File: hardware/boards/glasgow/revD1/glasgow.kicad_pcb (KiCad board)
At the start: 6 copper layers, 95 x 55 mm, 775 parts, among them J1 USB-C, J10 P1, J11 CLK_EXT, J12 FPGA_TP, J2 SWD, J3 COM, J4 SYNC, J5 JTAG, J6 LVDS, J7 P1, J8 P1, J9 P1, Q1 AO3401, Q2 AO3400, SW1 RST, U1 BL24C256A-SFRC, U10 74AXP1T45, U11 XccelaOPI, U12 XccelaOPI, U13 TLV62569PDRL, U14 TLV62569PDRL, U15 TLV61070ADBV, U16 APX811-40UG-7, U17 TLV77525DRL, U18 TLV62569PDRL, U19 TPS7A2033, U2 CY7C68013A-56LTX, U20 TPS22917DBV, U21 DAC43204, U22 LMR54406, U23 SY7208CABC, U24 TCA6416APW, U25 TCA6416APW, U26 74AXP1T45, U27 74AXP1T45, U28 TPS629203, U29 74AXP1T45, U3 TMP112xxDRL, U30 74AXP1T45, U31 74AXP1T45, U32 74AXP1T45, U33 NCP456R, U34 INA233, U35 74AXP1T45, U36 74AXP1T45, U37 TLV6001DCK, U38 74AXP1T45, U39 74AXP1T45, U4 FUSB302B01MPX, U40 TPS629203, U41 74AXP1T45, U42 74AXP1T45, U43 74AXP1T45, U44 74AXP1T45, U45 NCP456R, U46 INA233, U47 74AXP1T45, U48 74AXP1T45, U49 TLV6001DCK, U5 TPS259472ARPW, U50 74AXP1T45, U51 74AXP1T45, U52 TPS629203, U53 74AXP1T45, U54 74AXP1T45, U55 74AXP1T45, U56 74AXP1T45, U57 NCP456R, U58 INA233, U59 74AXP1T45, U6 STM32G031G6Ux, U60 74AXP1T45, U61 TLV6001DCK, U62 74AXP1T45, U63 74AXP1T45, U64 TPS629203, U65 74AXP1T45, U66 74AXP1T45, U67 74AXP1T45, U68 74AXP1T45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

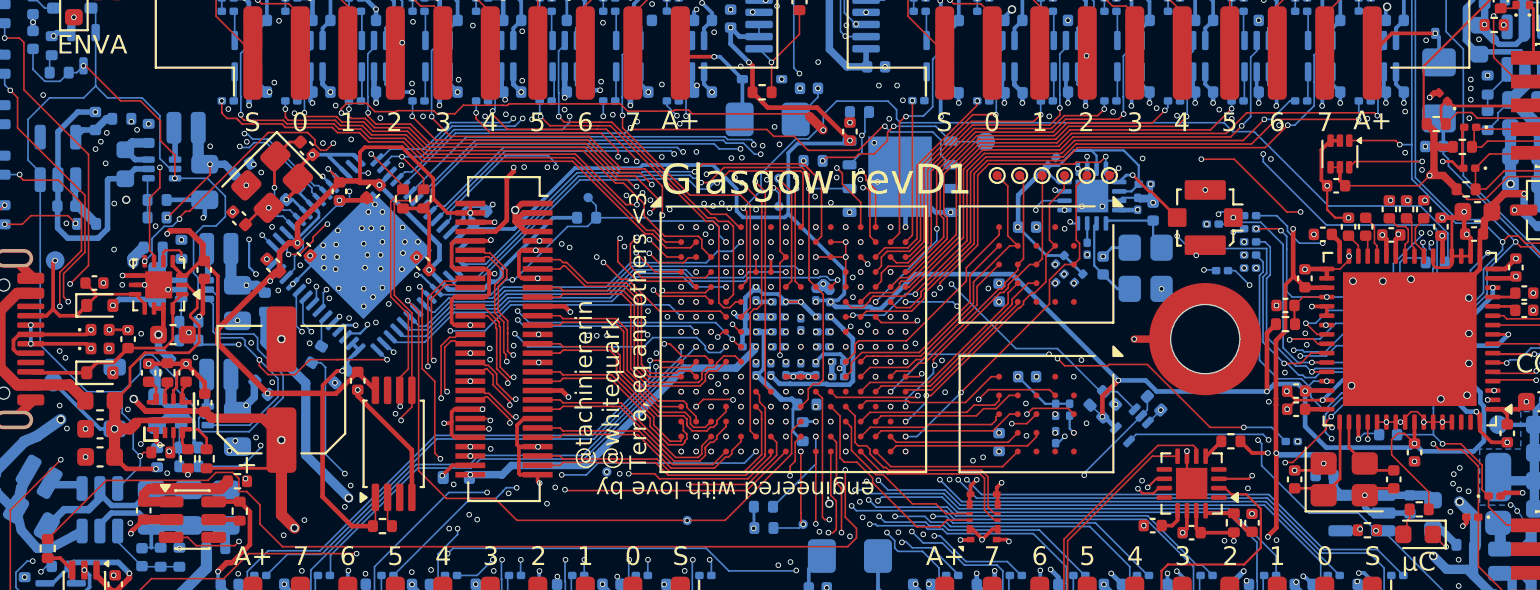
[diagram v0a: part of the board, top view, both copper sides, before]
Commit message: misc review changes
disconnect eFuse PG and add comments in schematic as to why
add slew-rate limiting resistor to NAFE clock
add esd diode to external clock output
fix USB D+/D- diff-pairs
update schematic to current date and set revision to D1
fix RAM balls B3/B4 assignment
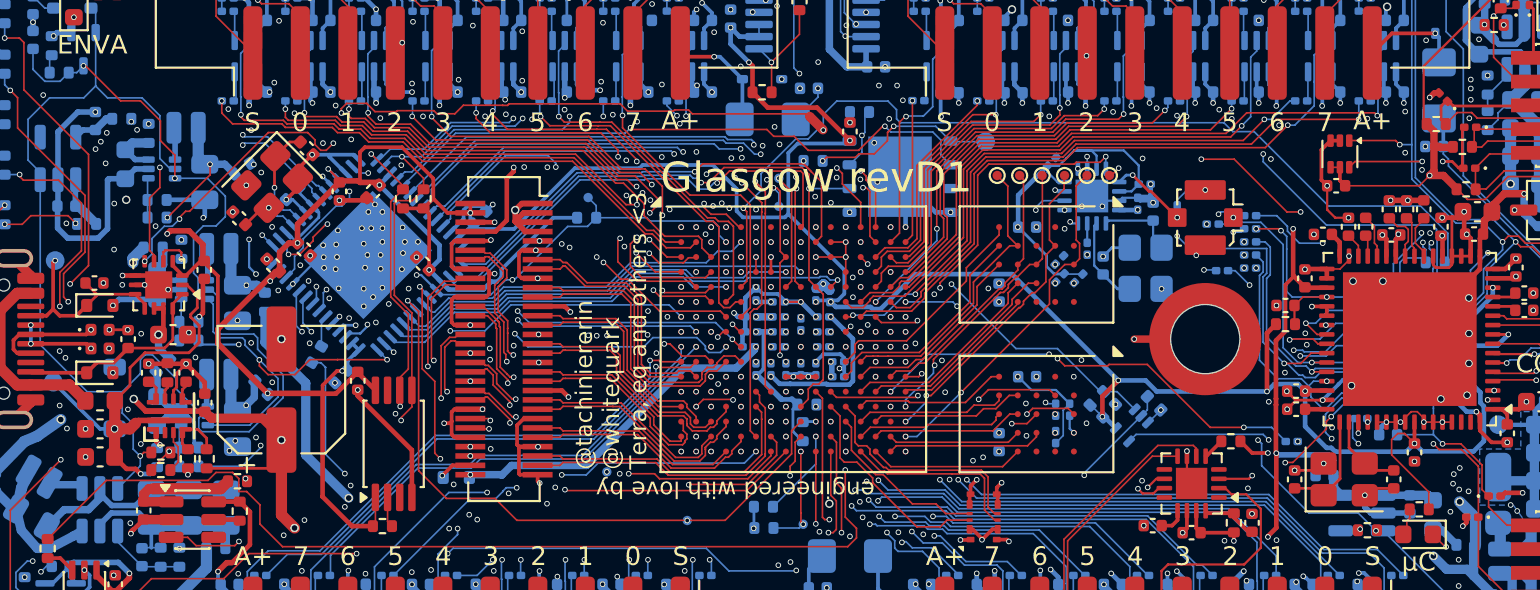
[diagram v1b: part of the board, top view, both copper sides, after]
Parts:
- added D120: 3.3V, Diode_SMD:D_0201_0603Metric, B.Cu at (184.8, 101.4)
- added R252: 0, Resistor_SMD:R_0402_1005Metric, F.Cu at (130.4, 115.2)
- added R26: 47, Resistor_SMD:R_0201_0603Metric, B.Cu at (194.6, 112.5)
- moved R263 1.47 mm to (178.3, 112.0), turned to 90 degrees
- moved R262 1.46 mm to (178.3, 113.4), turned to -90 degrees
- moved R265 0.98 mm to (178.5, 104.0)
- moved R264 0.97 mm to (178.5, 104.9)
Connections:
- U11 pad B3: Net-(R264-Pad1) -> Net-(R265-Pad1)
- U11 pad B4: Net-(R265-Pad1) -> Net-(R264-Pad1)
- U12 pad B3: Net-(R262-Pad1) -> Net-(R263-Pad1)
- U12 pad B4: Net-(R263-Pad1) -> Net-(R262-Pad1)
- U5 pad 3: /PG_{VBUS} -> Net-(U5-PG)
- U7 pad 52: /NAFE_CLK_{OUT} -> Net-(U7-GPIO9)
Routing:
- net +3V3: track 495.4 -> 492.3 mm
- net GND: track 416.1 -> 419.2 mm, vias 680 -> 676
- net +1V8: track 110.6 -> 113.4 mm
- net Net-(U5-PG): track 0.00 -> 2.28 mm
- net /ADC/SWDIO: track 31.5 -> 30.0 mm
- net /USB_P: track 29.2 -> 28.5 mm
- net Net-(U7-GPIO9): track 0.00 -> 0.20 mm, vias 0 -> 1
- net /FPGA/RAM + LVDS/CLK2: vias 1 -> 2
- net -15V: vias 10 -> 9
